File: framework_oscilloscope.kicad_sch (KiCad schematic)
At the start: 79 parts, among them IC1 FT232HL-REEL, IC10 93LC56BT-I_OT, IC2 ICE40UP5K-SG48I, IC3 ADC08060CIMTX_NOPB, IC7 OPA356AIDBVR, IC8 TLV77312PDBVR, IC9 LM4040C20IDBZT, J1 BNC, P1 USB_C_Plug_USB2.0, U9 TPS62A02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

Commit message: cleaned up schematics
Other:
- note added: "MECHANICAL"
- note removed: "Mechanical mounting"
- moved on the sheet: C10, C11, C12, C13, C14, C15, C16, C17, C18, C19, C2, C20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

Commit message: cleanup, and a little routing
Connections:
- net +VUSB is gone; now on net VBUS: C5.1, C6.1, R7.1, U9.3 (VIN)
- net +3V3: now also C27.1, Y1.1 (TRI-STATE), Y1.4 (VDD)
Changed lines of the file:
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@@
 	)
 	(junction
+		(at 243.84 105.41)
+		(diameter 0)
+		(color 0 0 0 0)
+	)
+	(junction
 		(at 208.28 72.39)
 		(diameter 0)
@@
 	(wire
 		(pts
+			(xy 241.3 105.41) (xy 243.84 105.41)
+		)
+		(stroke
+			(width 0)
+			(type default)
+		)
+	)
+	(wire
+		(pts
 			(xy 152.4 176.53) (xy 154.94 176.53)
 		)
@@
 	(wire
 		(pts
+			(xy 241.3 104.14) (xy 241.3 105.41)
+		)
+		(stroke
+			(width 0)
+			(type default)
+		)
+	)
+	(wire
+		(pts
 			(xy 21.59 290.83) (xy 27.94 290.83)
 		)
@@
 	(symbol
 		(lib_id "framework_oscilloscope:PLUS_3V3_BAR")
+		(at 21.59 288.29 180)
+		(unit 1)
+		(body_style 1)
+		(exclude_from_sim no)
+		(in_bom yes)
+		(on_board yes)
+		(in_pos_files yes)
+		(dnp no)
+		(property "Reference" "#PWR0321"
+			(at 21.59 288.29 0)
+			(hide yes)
+			(show_name no)
+			(do_not_autoplace no)
+			(effects
+				(font
+					(size 1.27 1.27)
+				)
+			)
+		)
+		(property "Value" "VBUS"
+			(at 21.59 284.48 0)
+			(show_name no)
+			(do_not_autoplace no)
+			(effects
+				(font
+					(size 1.27 1.27)
+				)
+			)
+		)
+		(property "Footprint" ""
+			(at 21.59 288.29 0)
+			(hide yes)
+			(show_name no)
+			(do_not_autoplace no)
+			(effects
+				(font
+					(size 1.27 1.27)
+				)
+			)
+		)
+		(property "Datasheet" ""
+			(at 21.59 288.29 0)
+			(show_name no)
+			(do_not_autoplace no)
+			(effects
+				(font
+					(size 1.27 1.27)
+				)
+			)
+		)
+		(property "Description" ""
+			(at 21.59 288.29 0)
+			(show_name no)
+			(do_not_autoplace no)
+			(effects
+				(font
+					(size 1.27 1.27)
+				)
+			)
+		)
+		(pin ""
+		)
+		(instances
+			(project "framework_oscilloscope"
+				(path "/cf9cb3b7-94d2-4f59-bc33-73600a6e7599"
+					(reference "#PWR0321")
+					(unit 1)
+				)
+			)
+		)
+	)
+	(symbol
+		(lib_id "framework_oscilloscope:PLUS_3V3_BAR")
 		(at 193.04 162.56 180)
 		(unit 1)
@@
 	)
 	(symbol
-		(lib_id "framework_oscilloscope:PLUS_VUSB")
-		(at 21.59 288.29 180)
-		(unit 1)
-		(body_style 1)
-		(exclude_from_sim no)
-		(in_bom yes)
-		(on_board yes)
-		(in_pos_files yes)
-		(dnp no)
-		(property "Reference" "#PWR0290"
-			(at 21.59 288.29 0)
-			(hide yes)
-			(show_name no)
-			(do_not_autoplace no)
-			(effects
-				(font
-					(size 1.27 1.27)
-				)
-			)
-		)
-		(property "Value" "+VUSB"
-			(at 21.59 284.48 0)
-			(show_name no)
-			(do_not_autoplace no)
-			(effects
-				(font
-					(size 1.27 1.27)
-				)
-			)
-		)
-		(property "Footprint" ""
-			(at 21.59 288.29 0)
-			(hide yes)
-			(show_name no)
-			(do_not_autoplace no)
-			(effects
-				(font
-					(size 1.27 1.27)
-				)
-			)
-		)
-		(property "Datasheet" ""
-			(at 21.59 288.29 0)
-			(show_name no)
-			(do_not_autoplace no)
-			(effects
-				(font
-					(size 1.27 1.27)
-				)
-			)
-		)
-		(property "Description" ""
-			(at 21.59 288.29 0)
-			(show_name no)
-			(do_not_autoplace no)
-			(effects
-				(font
-					(size 1.27 1.27)
-				)
-			)
-		)
-		(pin ""
-		)
-		(instances
-			(project "framework_oscilloscope"
-				(path "/cf9cb3b7-94d2-4f59-bc33-73600a6e7599"
-					(reference "#PWR0290")
-					(unit 1)
-				)
-			)
-		)
-	)
-	(symbol
 		(lib_id "framework_oscilloscope:C_Small")
 		(at 50.8 160.02 0)
@@
 					(unit 1)
 				)
+			)
+		)
+	)
+	(symbol
+		(lib_id "framework_oscilloscope:PLUS_3V3_BAR")
+		(at 241.3 104.14 180)
+		(unit 1)
+		(body_style 1)
+		(exclude_from_sim no)
+		(in_bom yes)
+		(on_board yes)
+		(in_pos_files yes)
+		(dnp no)
+		(property "Reference" "#PWR0322"
+			(at 241.3 104.14 0)
+			(hide yes)
+			(show_name no)
+			(do_not_autoplace no)
+			(effects
+				(font
+					(size 1.27 1.27)
+				)
+			)
+		)
+		(property "Value" "+3V3"
+			(at 241.3 100.33 0)
+			(show_name no)
+			(do_not_autoplace no)
+			(effects
+				(font
+					(size 1.27 1.27)
+				)
+			)
+		)
+		(property "Footprint" ""
+			(at 241.3 104.14 0)
+			(hide yes)
+			(show_name no)
+			(do_not_autoplace no)
+			(effects
+				(font
+					(size 1.27 1.27)
+				)
+			)
+		)
+		(property "Datasheet" ""
+			(at 241.3 104.14 0)
+			(show_name no)
+			(do_not_autoplace no)
+			(effects
+				(font
+					(size 1.27 1.27)
+				)
+			)
+		)
+		(property "Description" ""
+			(at 241.3 104.14 0)
+			(show_name no)
+			(do_not_autoplace no)
+			(effects
+				(font
+					(size 1.27 1.27)
+				)
+			)
+		)
+		(pin ""
+		)
+		(instances
+			(project "framework_oscilloscope"
+				(path "/cf9cb3b7-94d2-4f59-bc33-73600a6e7599"
+					(reference "#PWR0322")
+					(unit 1)
+				)

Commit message: small sch tweek, almost done routing
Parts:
- added C47: 100nF, framework_oscilloscope:0402_1005Metric_CAP, symbol framework_oscilloscope:C_Small
- C25: value 1uF -> 100nF
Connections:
- net +2V048: now also C47.1
- net GND: now also C47.2
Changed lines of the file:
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@@
 	)
 	(junction
+		(at 243.84 151.13)
+		(diameter 0)
+		(color 0 0 0 0)
+	)
+	(junction
 		(at 243.84 229.87)
 		(diameter 0)
@@
 	)
 	(junction
+		(at 247.65 156.21)
+		(diameter 0)
+		(color 0 0 0 0)
+	)
+	(junction
 		(at 48.26 132.08)
 		(diameter 0)
@@
 	(wire
 		(pts
+			(xy 247.65 156.21) (xy 247.65 160.02)
+		)
+		(stroke
+			(width 0)
+			(type default)
+		)
+	)
+	(wire
+		(pts
 			(xy 190.5 166.37) (xy 191.77 166.37)
 		)
@@
 	(wire
 		(pts
-			(xy 247.65 151.13) (xy 236.22 151.13)
+			(xy 247.65 151.13) (xy 243.84 151.13)
 		)
 		(stroke
@@
 	(wire
 		(pts
-			(xy 247.65 153.67) (xy 247.65 160.02)
+			(xy 247.65 153.67) (xy 247.65 156.21)
 		)
 		(stroke
@@
 	(wire
 		(pts
+			(xy 243.84 156.21) (xy 247.65 156.21)
+		)
+		(stroke
+			(width 0)
+			(type default)
+		)
+	)
+	(wire
+		(pts
 			(xy 120.65 27.94) (xy 133.35 27.94)
 		)
@@
 		)
 	)
+	(wire
+		(pts
+			(xy 243.84 151.13) (xy 236.22 151.13)
+		)
+		(stroke
+			(width 0)
+			(type default)
+		)
+	)
 	(polyline
 		(pts
@@
 		(dnp no)
 		(property "Reference" "C25"
-			(at 195.834 164.846 90)
+			(at 189.484 165.354 90)
 			(show_name no)
 			(do_not_autoplace no)
@@
 			)
 		)
-		(property "Value" "1uF"
-			(at 193.294 167.386 90)
+		(property "Value" "100nF"
+			(at 201.422 165.354 90)
 			(show_name no)
 			(do_not_autoplace no)
@@
 					(unit 1)
 				)
+			)
+		)
+	)
+	(symbol
+		(lib_id "framework_oscilloscope:C_Small")
+		(at 243.84 153.67 0)
+		(mirror y)
+		(unit 1)
+		(body_style 1)
+		(exclude_from_sim no)
+		(in_bom yes)
+		(on_board yes)
+		(in_pos_files yes)
+		(dnp no)
+		(property "Reference" "C47"
+			(at 241.554 154.178 0)
+			(show_name no)
+			(do_not_autoplace no)
+			(effects
+				(font
+					(size 1.27 1.27)
+				)
+				(justify left)
+			)
+		)
+		(property "Value" "100nF"
+			(at 241.808 151.892 0)
+			(show_name no)
+			(do_not_autoplace no)
+			(effects
+				(font
+					(size 1.27 1.27)
+				)
+				(justify left)
+			)
+		)
+		(property "Footprint" "framework_oscilloscope:0402_1005Metric_CAP"
+			(at 243.84 153.67 0)
+			(hide yes)
+			(show_name no)
+			(do_not_autoplace no)
+			(effects
+				(font
+					(size 1.27 1.27)
+				)
+			)
+		)
+		(property "Datasheet" ""
+			(at 243.84 153.67 0)
+			(show_name no)
+			(do_not_autoplace no)
+			(effects
+				(font
+					(size 1.27 1.27)
+				)
+			)
+		)
+		(property "Description" ""
+			(at 243.84 153.67 0)
+			(show_name no)
+			(do_not_autoplace no)
+			(effects
+				(font
+					(size 1.27 1.27)
+				)
+			)
+		)
+		(pin "2"
+		)
+		(pin "1"
+		)
+		(instances
+			(project "framework_oscilloscope"
+				(path "/cf9cb3b7-94d2-4f59-bc33-73600a6e7599"
+					(reference "C47")
+					(unit 1)
+				)

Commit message: done routing
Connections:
- net GND: now also C26.2, Y2.2 (GND)
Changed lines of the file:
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@@
 	)
 	(junction
+		(at 91.44 27.94)
+		(diameter 0)
+		(color 0 0 0 0)
+	)
+	(junction
 		(at 227.33 184.15)
 		(diameter 0)
@@
 	(wire
 		(pts
+			(xy 91.44 27.94) (xy 91.44 29.21)
+		)
+		(stroke
+			(width 0)
+			(type default)
+		)
+	)
+	(wire
+		(pts
 			(xy 243.84 111.76) (xy 243.84 113.03)
 		)
@@
 					(unit 1)
 				)
+			)
+		)
+	)
+	(symbol
+		(lib_id "framework_oscilloscope:GND")
+		(at 91.44 29.21 0)
+		(unit 1)
+		(body_style 1)
+		(exclude_from_sim no)
+		(in_bom yes)
+		(on_board yes)
+		(in_pos_files yes)
+		(dnp no)
+		(property "Reference" "#PWR027"
+			(at 91.44 35.56 0)
+			(hide yes)
+			(show_name no)
+			(do_not_autoplace no)
+			(effects
+				(font
+					(size 1.27 1.27)
+				)
+			)
+		)
+		(property "Value" "GND"
+			(at 91.567 33.6042 0)
+			(show_name no)
+			(do_not_autoplace no)
+			(effects
+				(font
+					(size 1.27 1.27)
+				)
+			)
+		)
+		(property "Footprint" ""
+			(at 91.44 29.21 0)
+			(hide yes)
+			(show_name no)
+			(do_not_autoplace no)
+			(effects
+				(font
+					(size 1.27 1.27)
+				)
+			)
+		)
+		(property "Datasheet" ""
+			(at 91.44 29.21 0)
+			(show_name no)
+			(do_not_autoplace no)
+			(effects
+				(font
+					(size 1.27 1.27)
+				)
+			)
+		)
+		(property "Description" ""
+			(at 91.44 29.21 0)
+			(show_name no)
+			(do_not_autoplace no)
+			(effects
+				(font
+					(size 1.27 1.27)
+				)
+			)
+		)
+		(pin "1"
+		)
+		(instances
+			(project "framework_oscilloscope"
+				(path "/cf9cb3b7-94d2-4f59-bc33-73600a6e7599"
+					(reference "#PWR027")
+					(unit 1)
+				)

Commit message: fixed emc errors, fixed drc errors
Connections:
- no-connect marks 7 -> 25
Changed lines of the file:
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@@
+	)
+	(no_connect
+		(at 113.03 160.02)
+	)
+	(no_connect
+		(at 113.03 165.1)
+	)
+	(no_connect
+		(at 67.31 175.26)
 	)
 	(no_connect
 		(at 133.35 30.48)
+	)
+	(no_connect
+		(at 67.31 182.88)
+	)
+	(no_connect
+		(at 67.31 195.58)
+	)
+	(no_connect
+		(at 67.31 205.74)
+	)
+	(no_connect
+		(at 67.31 208.28)
+	)
+	(no_connect
+		(at 67.31 213.36)
+	)
+	(no_connect
+		(at 67.31 200.66)
+	)
+	(no_connect
+		(at 67.31 215.9)
+	)
+	(no_connect
+		(at 67.31 177.8)
+	)
+	(no_connect
+		(at 67.31 193.04)
+	)
+	(no_connect
+		(at 67.31 198.12)
+	)
+	(no_connect
+		(at 67.31 180.34)
 	)
 	(no_connect
@@
 	)
 	(no_connect
+		(at 67.31 187.96)
+	)
+	(no_connect
 		(at 173.99 40.64)
 	)
@@
 		(at 173.99 50.8)
 	)
+	(no_connect
+		(at 67.31 203.2)
+	)
+	(no_connect
+		(at 67.31 218.44)
+	)
+	(no_connect
+		(at 67.31 185.42)
+	)
 	(wire

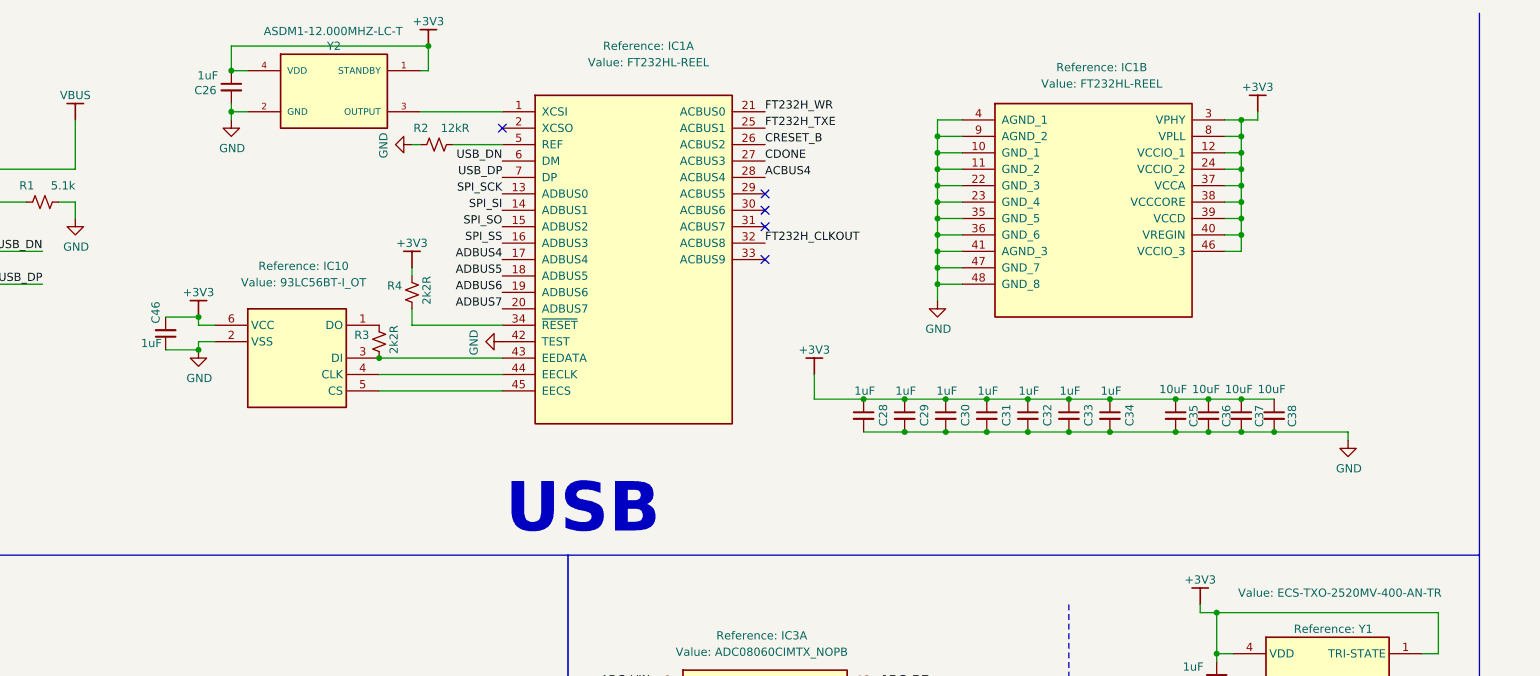
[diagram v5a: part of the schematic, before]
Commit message: added pull ups to eeprom->ftdi spi, as per reference design (tri state pins on FT232 SPI)
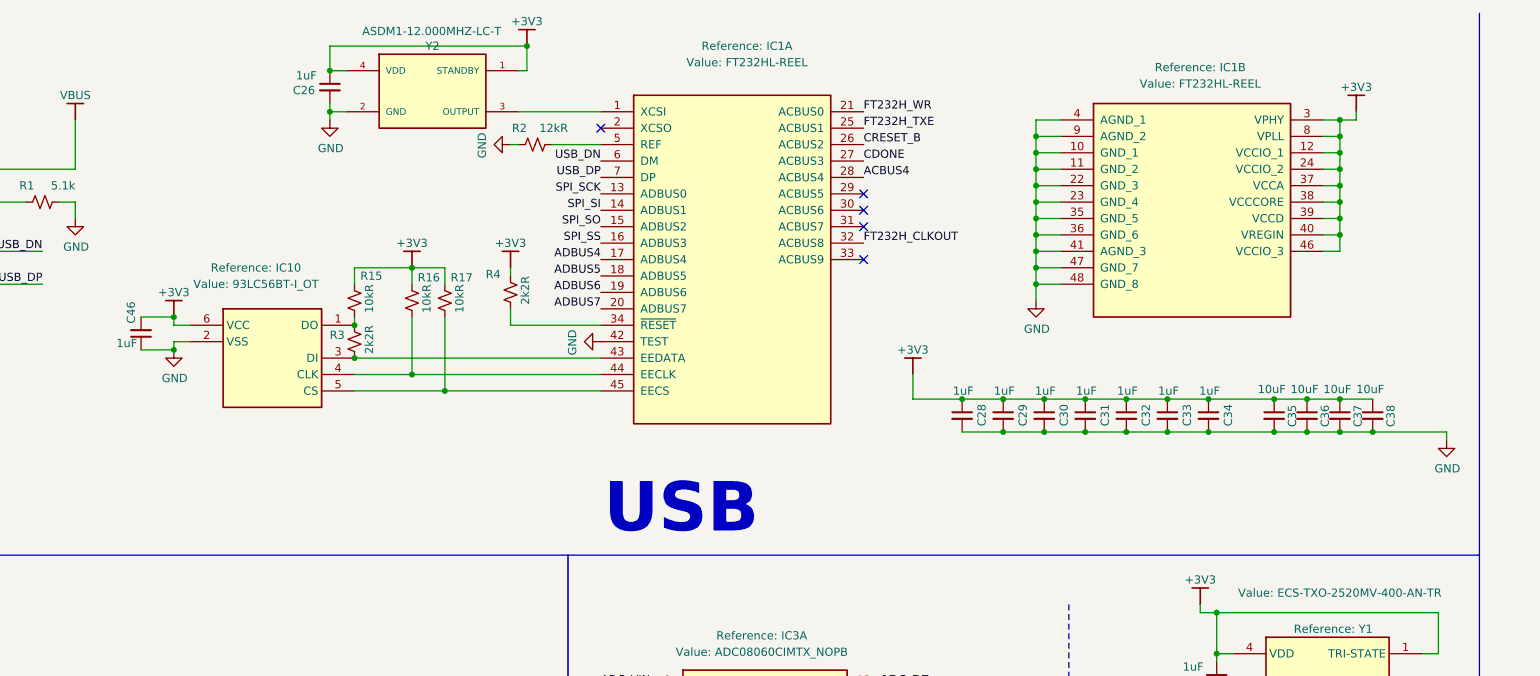
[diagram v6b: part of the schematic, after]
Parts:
- added R15, R16, R17: 10kR, framework_oscilloscope:0402_1005Metric, symbol framework_oscilloscope:R_Small_US
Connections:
- net +3V3: now also R15.2, R16.2, R17.2
- net at IC1.44 (EECLK), IC10.4 (CLK): now also R16.1
- net at IC1.45 (EECS), IC10.5 (CS): now also R17.1
- net at IC10.1 (DO), R3.2: now also R15.1
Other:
- moved on the sheet: C26, C28, C29, C30, C31, C32, C33, C34, C35, C36, C37, C38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
